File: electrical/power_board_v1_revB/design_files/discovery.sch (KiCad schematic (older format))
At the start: 18 parts, among them J1 Conn_02x04_CPU, J2 Conn_02x04_PCIe, J3 Conn_02x04_CPU, J4 Conn_02x04_PCIe, J5 Conn_02x04_PCIe, J6 Conn_02x04_PCIe

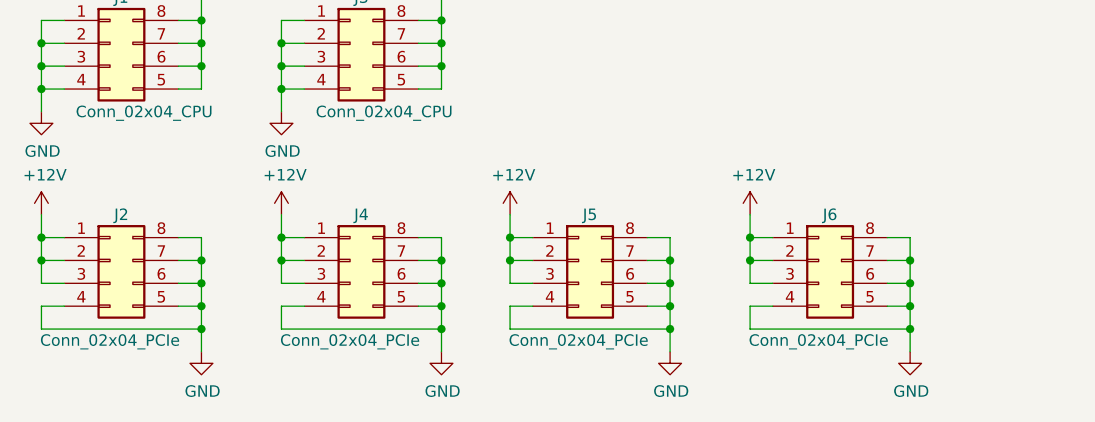
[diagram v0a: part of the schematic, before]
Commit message: Improvement
PCI connectors on the board have been modified into 2x3pins (2x4 pins originally).
Design and production files have been updated
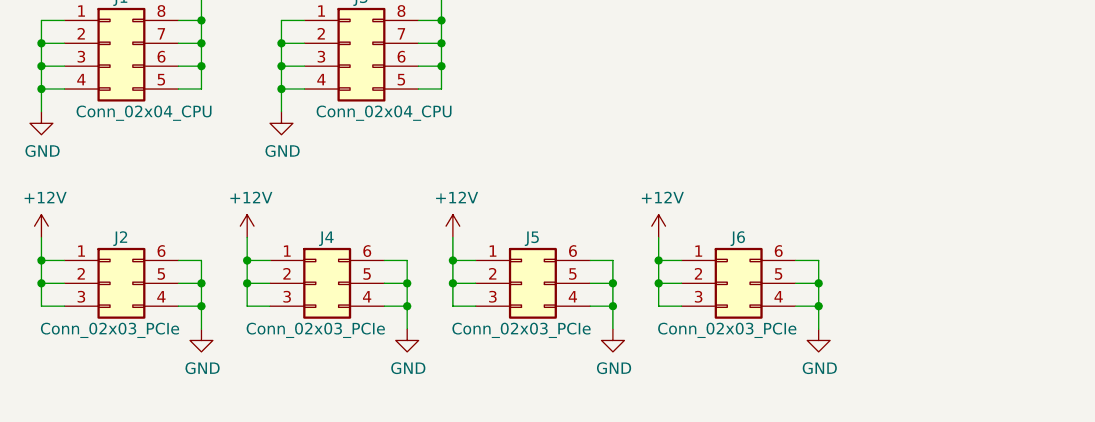
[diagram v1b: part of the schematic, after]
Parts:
- removed J2, J4, J5, J6: Conn_02x04_PCIe, footprint_cts:CONN_02x04_4.2mm, symbol Connector_Generic:Conn_02x04_Counter_Clockwise
- added J2, J4, J5, J6: Conn_02x03_PCIe, discovery:CONN_02x03_4.2mm, symbol Connector_Generic:Conn_02x03_Counter_Clockwise
- J1, J3: footprint footprint_cts:CONN_02x04_4.2mm -> discovery:CONN_02x04_4.2mm
- W1, W2, W3, W4: footprint TestPoint:TestPoint_Plated_Hole_D4.0mm -> discovery:FixingPoint_Plated_Hole_D4.0mm
- W10, W11, W12, W5, W6, W7, W8, W9: footprint footprint_cts:fixing_hole -> discovery:fixing_hole
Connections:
- net +12V: now also J2.1 (Pin_1), J2.2 (Pin_2), J2.3 (Pin_3), J4.1 (Pin_1), J4.2 (Pin_2), J4.3 (Pin_3), J5.1 (Pin_1), J5.2 (Pin_2), J5.3 (Pin_3), J6.1 (Pin_1), J6.2 (Pin_2), J6.3 (Pin_3)
- net GND: now also J2.4 (Pin_4), J2.5 (Pin_5), J2.6 (Pin_6), J4.4 (Pin_4), J4.5 (Pin_5), J4.6 (Pin_6), J5.4 (Pin_4), J5.5 (Pin_5), J5.6 (Pin_6), J6.4 (Pin_4), J6.5 (Pin_5), J6.6 (Pin_6)
